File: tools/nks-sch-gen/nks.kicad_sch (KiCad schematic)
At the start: 20 parts, among them J1 microSD, J2 DevKit-J1, J3 DevKit-J3, SW1 SW_SPDT, U2 RTC_DS3231+AT24C32, U3 SHT30, U4 TPS22918

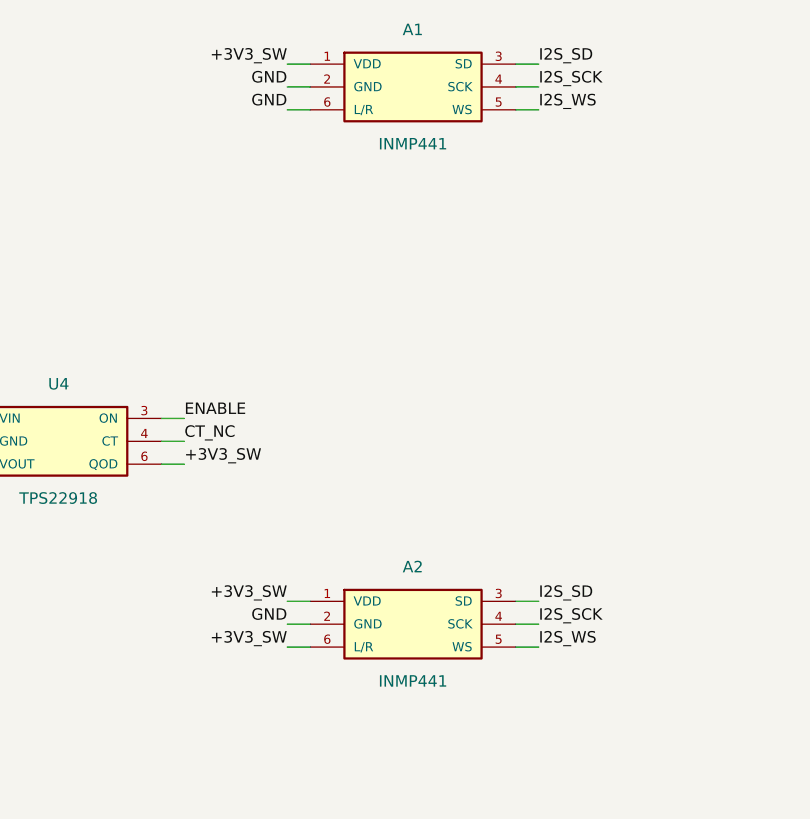
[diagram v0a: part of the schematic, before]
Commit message: Serigrafia de montaje + texto identificativo NkS. DRC 0/0/0 limpio.
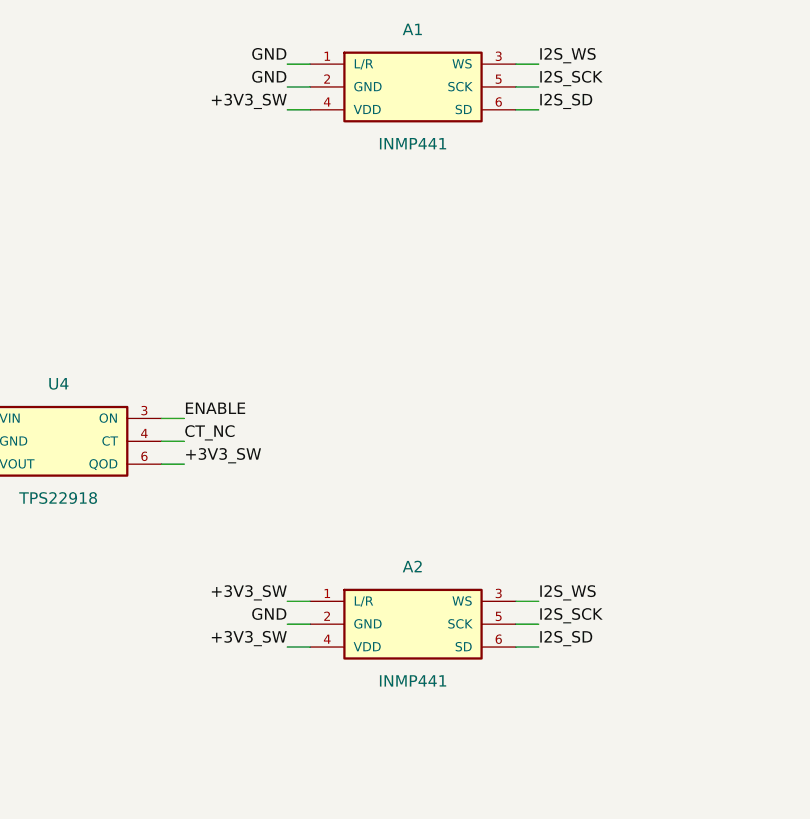
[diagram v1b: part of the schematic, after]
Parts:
- A1, A2: footprint Connector_PinHeader_2.54mm:PinHeader_1x06_P2.54mm_Vertical -> Connector_PinHeader_2.54mm:PinHeader_2x03_P2.54mm_Vertical
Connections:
- net +3V3_SW: now also A1.4 (VDD), A2.4 (VDD); no longer A1.1 (VDD), A2.6 (L/R)
- net GND: now also A1.1 (L/R); no longer A1.6 (L/R)
- net I2S_SCK: now also A1.5 (SCK), A2.5 (SCK); no longer A1.4 (SCK), A2.4 (SCK)
- net I2S_SD: now also A1.6 (SD), A2.6 (SD); no longer A1.3 (SD), A2.3 (SD)
- net I2S_WS: now also A1.3 (WS), A2.3 (WS); no longer A1.5 (WS), A2.5 (WS)
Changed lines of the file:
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@@
     (property "Reference" "A1" (at 142.240 22.860 0) (effects (font (size 1.27 1.27))))
     (property "Value" "INMP441" (at 142.240 35.560 0) (effects (font (size 1.27 1.27))))
-    (property "Footprint" "Connector_PinHeader_2.54mm:PinHeader_1x06_P2.54mm_Vertical" (at 142.240 29.210 0) (effects (font (size 1.27 1.27)) hide))
+    (property "Footprint" "Connector_PinHeader_2.54mm:PinHeader_2x03_P2.54mm_Vertical" (at 142.240 29.210 0) (effects (font (size 1.27 1.27)) hide))
     (pin "1")
     (pin "2")
-    (pin "6")
     (pin "3")
     (pin "4")
     (pin "5")
+    (pin "6")
     (instances (project "nks" (path "/ff07ce8f-c3d4-45e3-8c6f-5cb7c24c6ede" (reference "A1") (unit 1))))
   )
   (wire (pts (xy 130.810 26.670) (xy 128.270 26.670))
     (stroke (width 0) (type default)))
-  (label "+3V3_SW" (at 128.270 26.670 180) (effects (font (size 1.27 1.27)) (justify right bottom)))
+  (label "GND" (at 128.270 26.670 180) (effects (font (size 1.27 1.27)) (justify right bottom)))
   (wire (pts (xy 130.810 29.210) (xy 128.270 29.210))
     (stroke (width 0) (type default)))
@@
   (wire (pts (xy 130.810 31.750) (xy 128.270 31.750))
     (stroke (width 0) (type default)))
-  (label "GND" (at 128.270 31.750 180) (effects (font (size 1.27 1.27)) (justify right bottom)))
+  (label "+3V3_SW" (at 128.270 31.750 180) (effects (font (size 1.27 1.27)) (justify right bottom)))
   (wire (pts (xy 153.670 26.670) (xy 156.210 26.670))
     (stroke (width 0) (type default)))
-  (label "I2S_SD" (at 156.210 26.670 0) (effects (font (size 1.27 1.27)) (justify left bottom)))
+  (label "I2S_WS" (at 156.210 26.670 0) (effects (font (size 1.27 1.27)) (justify left bottom)))
   (wire (pts (xy 153.670 29.210) (xy 156.210 29.210))
     (stroke (width 0) (type default)))
@@
   (wire (pts (xy 153.670 31.750) (xy 156.210 31.750))
     (stroke (width 0) (type default)))
-  (label "I2S_WS" (at 156.210 31.750 0) (effects (font (size 1.27 1.27)) (justify left bottom)))
+  (label "I2S_SD" (at 156.210 31.750 0) (effects (font (size 1.27 1.27)) (justify left bottom)))
   (symbol
     (lib_id "nks:A2")
@@
     (property "Reference" "A2" (at 142.240 82.550 0) (effects (font (size 1.27 1.27))))
     (property "Value" "INMP441" (at 142.240 95.250 0) (effects (font (size 1.27 1.27))))
-    (property "Footprint" "Connector_PinHeader_2.54mm:PinHeader_1x06_P2.54mm_Vertical" (at 142.240 88.900 0) (effects (font (size 1.27 1.27)) hide))
+    (property "Footprint" "Connector_PinHeader_2.54mm:PinHeader_2x03_P2.54mm_Vertical" (at 142.240 88.900 0) (effects (font (size 1.27 1.27)) hide))
     (pin "1")
     (pin "2")
-    (pin "6")
     (pin "3")
     (pin "4")
     (pin "5")
+    (pin "6")
     (instances (project "nks" (path "/ff07ce8f-c3d4-45e3-8c6f-5cb7c24c6ede" (reference "A2") (unit 1))))
   )
@@
   (wire (pts (xy 153.670 86.360) (xy 156.210 86.360))
     (stroke (width 0) (type default)))
-  (label "I2S_SD" (at 156.210 86.360 0) (effects (font (size 1.27 1.27)) (justify left bottom)))
+  (label "I2S_WS" (at 156.210 86.360 0) (effects (font (size 1.27 1.27)) (justify left bottom)))
   (wire (pts (xy 153.670 88.900) (xy 156.210 88.900))
     (stroke (width 0) (type default)))
@@
   (wire (pts (xy 153.670 91.440) (xy 156.210 91.440))
     (stroke (width 0) (type default)))
-  (label "I2S_WS" (at 156.210 91.440 0) (effects (font (size 1.27 1.27)) (justify left bottom)))
+  (label "I2S_SD" (at 156.210 91.440 0) (effects (font (size 1.27 1.27)) (justify left bottom)))
   (symbol
     (lib_id "nks:J1")
